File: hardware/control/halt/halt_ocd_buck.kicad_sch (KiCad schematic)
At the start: 14 parts, among them U9 LM311

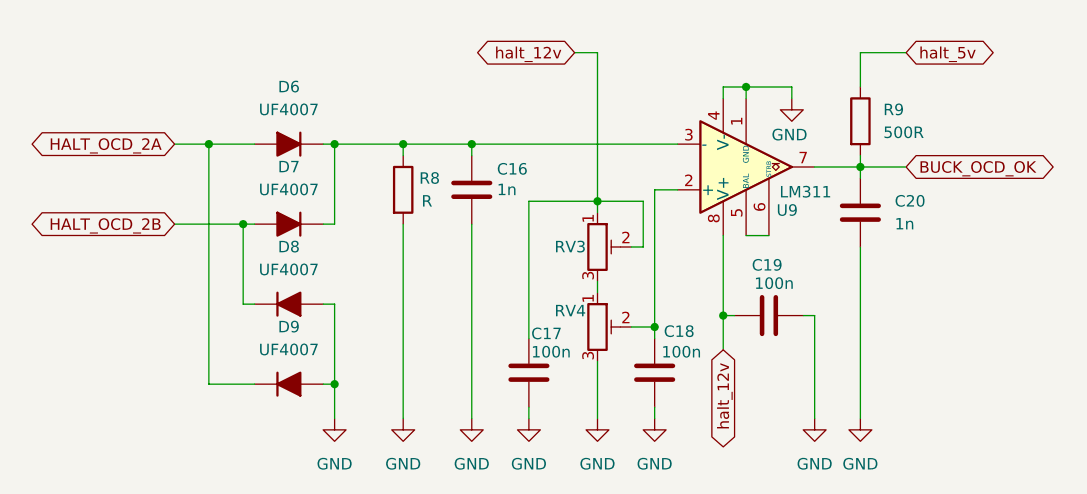
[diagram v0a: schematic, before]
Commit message: add progress on main drive controller and switch to hiearchical labels
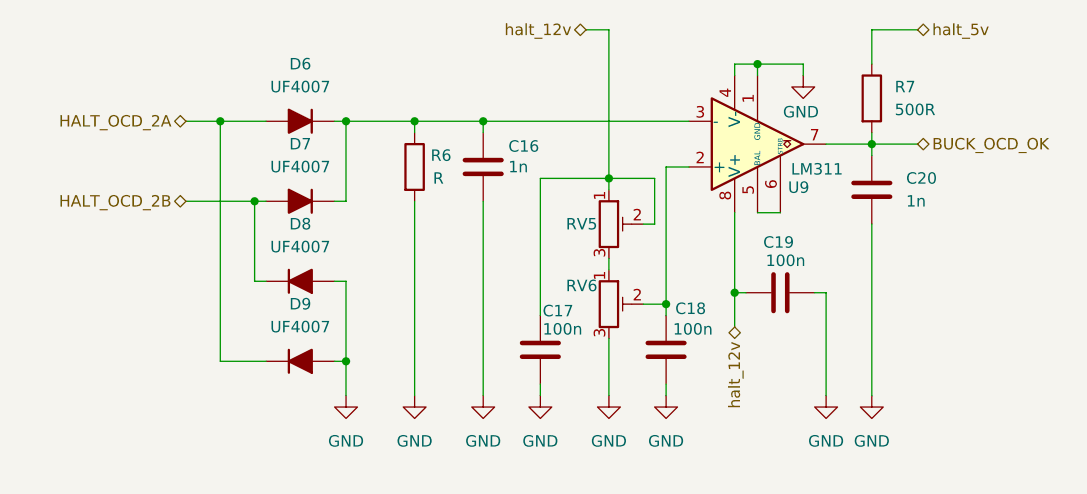
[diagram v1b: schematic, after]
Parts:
- removed R8: R, symbol Device:R
- removed R9: 500R, symbol Device:R
- removed RV3, RV4: R_Potentiometer_Trim, symbol Device:R_Potentiometer_Trim
- added R6: R, symbol Device:R
- added R7: 500R, symbol Device:R
- added RV5, RV6: R_Potentiometer_Trim, symbol Device:R_Potentiometer_Trim
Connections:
- net BUCK_OCD_OK: now also R7.2
- net GND: now also R6.2, RV6.3
- net halt_12v: now also RV5.1, RV5.2
- net halt_5v: now also R7.1
- net at C16.1, D6.1 (K), D7.1 (K)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: now also R6.1
- net at C18.1, U9.2 (+): now also RV6.2
- new net: RV5.3, RV6.1

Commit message: update right about freaking everything
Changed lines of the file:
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@@
 	(wire
 		(pts
-			(xy 162.56 95.25) (xy 165.1 95.25)
+			(xy 162.56 96.52) (xy 165.1 96.52)
 		)
 		(stroke
@@
 		)
 		(stroke
+			(width 0)
+			(type default)
+		)
+	)
+	(wire
+		(pts
+			(xy 162.56 96.52) (xy 162.56 95.25)
+		)
+		(stroke
+			(width 0)
+			(type default)
+		)
+	)
+	(wire
+		(pts
+			(xy 165.1 96.52) (xy 165.1 95.25)
+		)
+		(stroke
